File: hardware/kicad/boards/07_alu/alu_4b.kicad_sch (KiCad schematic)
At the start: 6 parts, among them U27 74HC86, U29 74HC00, U30 74ACT283

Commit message: schematics: implemented adder(lut3, lut3, h(cin)) design
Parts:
- removed C32, C34: 100nF, Capacitor_SMD:C_0603_1608Metric, symbol Device:C
- removed U27: 74HC86, Package_SO:SOIC-14_3.9x8.7mm_P1.27mm, symbol 74xx:74HC86
- removed U29: 74HC00, Package_SO:SOIC-14_3.9x8.7mm_P1.27mm, symbol 74xx:74HC00
- added C4: 100nF, Capacitor_SMD:C_0603_1608Metric, symbol Device:C
- added U4: 74LS32, Package_SO:SOIC-14_3.9x8.7mm_P1.27mm, symbol 74xx:74LS32
- renumbered C30 to C3, U30 to U3
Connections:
- net logA3 is gone; now on net aeff3: U3.12 (A4)
- net logB3 is gone; now on net beff3: U3.11 (B4)
- net GND: now also C4.1, U4.7 (GND)
- net VCC: now also C4.2, U4.14 (VCC)
- net out-4b0: now also U4.1
- net out-4b1: now also U4.2
- net out-4b2: now also U4.4
- net sum3: now also U4.5
- new net: U4.10, U4.6
- new net: U4.12, U4.8
- new net: U4.3, U4.9
- new net Z_in: U4.13
- new net Z_out: U4.11

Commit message: checkpoint: most recent 16b cell: ~120mm by 120mm
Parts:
- removed C4: 100nF, Capacitor_SMD:C_0603_1608Metric, symbol Device:C
- removed U4: 74LS32, Package_SO:SOIC-14_3.9x8.7mm_P1.27mm, symbol 74xx:74LS32

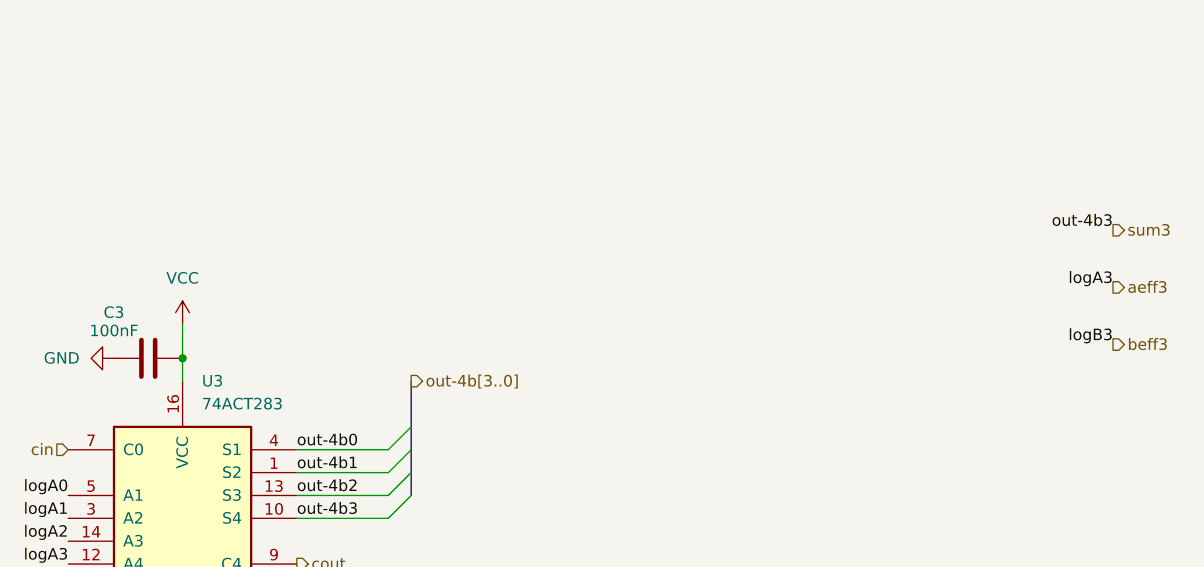
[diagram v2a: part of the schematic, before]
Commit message: fix: resolved kicad erc tests to 0
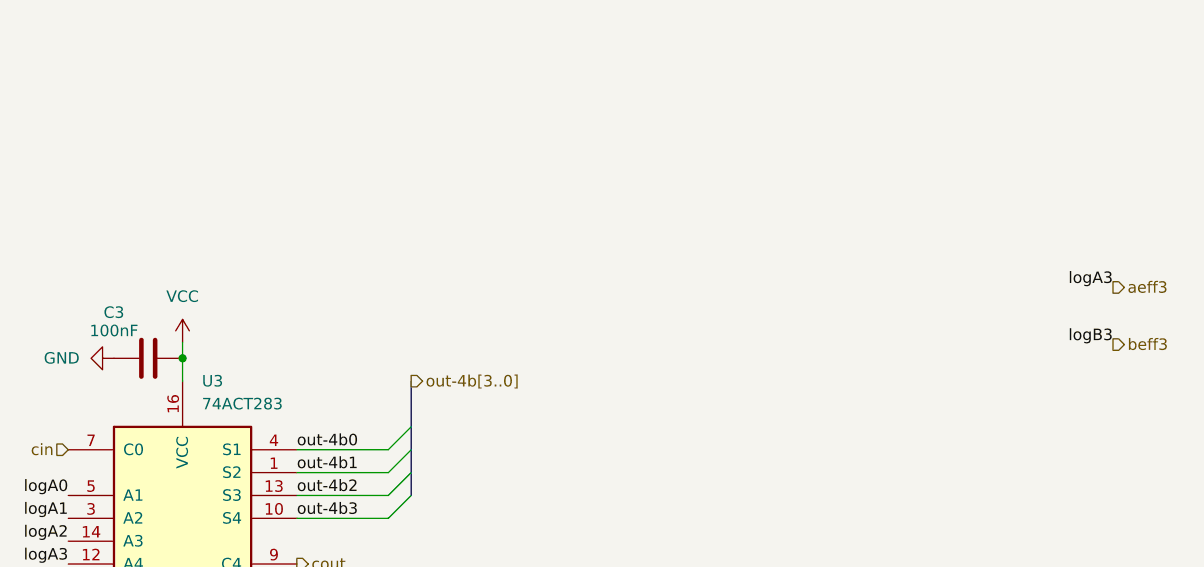
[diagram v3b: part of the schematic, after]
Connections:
- net sum3 renamed out-4b3
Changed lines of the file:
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@@
 	(wire
 		(pts
-			(xy 123.19 74.168) (xy 123.19 77.978)
+			(xy 123.19 76.2) (xy 123.19 77.978)
 		)
 		(stroke
@@
 			)
 			(justify left bottom)
-		)
-	)
-	(label "out-4b3"
-		(at 226.568 63.754 180)
-		(effects
-			(font
-				(size 1.27 1.27)
-			)
-			(justify right bottom)
 		)
 	)
@@
 			)
 			(justify right)
-		)
-	)
-	(hierarchical_label "sum3"
-		(shape output)
-		(at 226.568 63.754 0)
-		(effects
-			(font
-				(size 1.27 1.27)
-			)
-			(justify left)
 		)
 	)
@@
 		(instances
 			(project "07_alu"
-				(path "/bf03590f-4078-420b-ac5f-55731d384371/37660c86-5797-4efb-8a81-fa8883212b3f"
-					(reference "U8")
-					(unit 1)
-				)
-				(path "/bf03590f-4078-420b-ac5f-55731d384371/81d21ac7-f952-4f69-8db2-8103aa3e827d"
-					(reference "U7")
-					(unit 1)
-				)
 				(path "/bf03590f-4078-420b-ac5f-55731d384371/e403b414-62b1-4f5c-9e67-04653a2813f4"
 					(reference "U5")
@@
 	(symbol
 		(lib_id "power:VCC")
-		(at 123.19 74.168 0)
+		(at 123.19 76.2 0)
 		(unit 1)
 		(body_style 1)
@@
 		(fields_autoplaced yes)
 		(property "Reference" "#PWR012"
-			(at 123.19 77.978 0)
+			(at 123.19 80.01 0)
 			(hide yes)
 			(show_name no)
@@
 		)
 		(property "Value" "VCC"
-			(at 123.19 69.088 0)
+			(at 123.19 71.12 0)
 			(show_name no)
 			(do_not_autoplace no)
@@
 		)
 		(property "Footprint" ""
-			(at 123.19 74.168 0)
+			(at 123.19 76.2 0)
 			(hide yes)
 			(show_name no)
@@
 		)
 		(property "Datasheet" ""
-			(at 123.19 74.168 0)
+			(at 123.19 76.2 0)
 			(hide yes)
 			(show_name no)
@@
 		)
 		(property "Description" "Power symbol creates a global label with name \"VCC\""
-			(at 123.19 74.168 0)
+			(at 123.19 76.2 0)
 			(hide yes)
 			(show_name no)
@@
 		(instances
 			(project "07_alu"
-				(path "/bf03590f-4078-420b-ac5f-55731d384371/37660c86-5797-4efb-8a81-fa8883212b3f"
-					(reference "#PWR021")
-					(unit 1)
-				)
-				(path "/bf03590f-4078-420b-ac5f-55731d384371/81d21ac7-f952-4f69-8db2-8103aa3e827d"
-					(reference "#PWR018")
-					(unit 1)
-				)
 				(path "/bf03590f-4078-420b-ac5f-55731d384371/e403b414-62b1-4f5c-9e67-04653a2813f4"
 					(reference "#PWR015")
@@
 		(instances
 			(project "07_alu"
-				(path "/bf03590f-4078-420b-ac5f-55731d384371/37660c86-5797-4efb-8a81-fa8883212b3f"
-					(reference "#PWR022")
-					(unit 1)
-				)
-				(path "/bf03590f-4078-420b-ac5f-55731d384371/81d21ac7-f952-4f69-8db2-8103aa3e827d"
-					(reference "#PWR019")
-					(unit 1)
-				)
 				(path "/bf03590f-4078-420b-ac5f-55731d384371/e403b414-62b1-4f5c-9e67-04653a2813f4"
 					(reference "#PWR016")
@@
 		(instances
 			(project "07_alu"
-				(path "/bf03590f-4078-420b-ac5f-55731d384371/37660c86-5797-4efb-8a81-fa8883212b3f"
-					(reference "C6")
-					(unit 1)
-				)
-				(path "/bf03590f-4078-420b-ac5f-55731d384371/81d21ac7-f952-4f69-8db2-8103aa3e827d"
-					(reference "C5")
-					(unit 1)
-				)
 				(path "/bf03590f-4078-420b-ac5f-55731d384371/e403b414-62b1-4f5c-9e67-04653a2813f4"
 					(reference "C4")
@@
 		(instances
 			(project "07_alu"
-				(path "/bf03590f-4078-420b-ac5f-55731d384371/37660c86-5797-4efb-8a81-fa8883212b3f"
-					(reference "#PWR020")
-					(unit 1)
-				)
-				(path "/bf03590f-4078-420b-ac5f-55731d384371/81d21ac7-f952-4f69-8db2-8103aa3e827d"
-					(reference "#PWR017")
-					(unit 1)
-				)
 				(path "/bf03590f-4078-420b-ac5f-55731d384371/e403b414-62b1-4f5c-9e67-04653a2813f4"
 					(reference "#PWR014")
@@
 					(page "5")
 				)
-				(path "/bf03590f-4078-420b-ac5f-55731d384371/81d21ac7-f952-4f69-8db2-8103aa3e827d"
-					(page "14")
-				)
-				(path "/bf03590f-4078-420b-ac5f-55731d384371/37660c86-5797-4efb-8a81-fa8883212b3f"
-					(page "23")
-				)
 			)
 		)
@@
 					(page "7")
 				)
-				(path "/bf03590f-4078-420b-ac5f-55731d384371/81d21ac7-f952-4f69-8db2-8103aa3e827d"
-					(page "16")
-				)
-				(path "/bf03590f-4078-420b-ac5f-55731d384371/37660c86-5797-4efb-8a81-fa8883212b3f"
-					(page "25")
-				)
 			)
 		)
@@
 					(page "11")
 				)
-				(path "/bf03590f-4078-420b-ac5f-55731d384371/81d21ac7-f952-4f69-8db2-8103aa3e827d"
-					(page "20")
-				)
-				(path "/bf03590f-4078-420b-ac5f-55731d384371/37660c86-5797-4efb-8a81-fa8883212b3f"
-					(page "29")
-				)
 			)
 		)
@@
 					(page "4")
 				)
-				(path "/bf03590f-4078-420b-ac5f-55731d384371/81d21ac7-f952-4f69-8db2-8103aa3e827d"
-					(page "13")
-				)
-				(path "/bf03590f-4078-420b-ac5f-55731d384371/37660c86-5797-4efb-8a81-fa8883212b3f"
-					(page "22")
-				)
 			)
 		)
@@
 					(page "10")
 				)
-				(path "/bf03590f-4078-420b-ac5f-55731d384371/81d21ac7-f952-4f69-8db2-8103aa3e827d"
-					(page "19")
-				)
-				(path "/bf03590f-4078-420b-ac5f-55731d384371/37660c86-5797-4efb-8a81-fa8883212b3f"
-					(page "28")
-				)
 			)
 		)
@@
 					(page "9")
 				)
-				(path "/bf03590f-4078-420b-ac5f-55731d384371/81d21ac7-f952-4f69-8db2-8103aa3e827d"
-					(page "18")
-				)
-				(path "/bf03590f-4078-420b-ac5f-55731d384371/37660c86-5797-4efb-8a81-fa8883212b3f"
-					(page "27")
-				)
 			)
 		)
@@
 					(page "8")
 				)
-				(path "/bf03590f-4078-420b-ac5f-55731d384371/81d21ac7-f952-4f69-8db2-8103aa3e827d"
-					(page "17")
-				)
-				(path "/bf03590f-4078-420b-ac5f-55731d384371/37660c86-5797-4efb-8a81-fa8883212b3f"
-					(page "26")
-				)
 			)
 		)
@@
 					(page "6")
 				)
-				(path "/bf03590f-4078-420b-ac5f-55731d384371/81d21ac7-f952-4f69-8db2-8103aa3e827d"
-					(page "15")
-				)
-				(path "/bf03590f-4078-420b-ac5f-55731d384371/37660c86-5797-4efb-8a81-fa8883212b3f"
-					(page "24")
-				)
-			)
+			)
